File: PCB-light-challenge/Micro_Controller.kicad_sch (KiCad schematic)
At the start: 6 parts, among them J2 Screw_Terminal_01x20

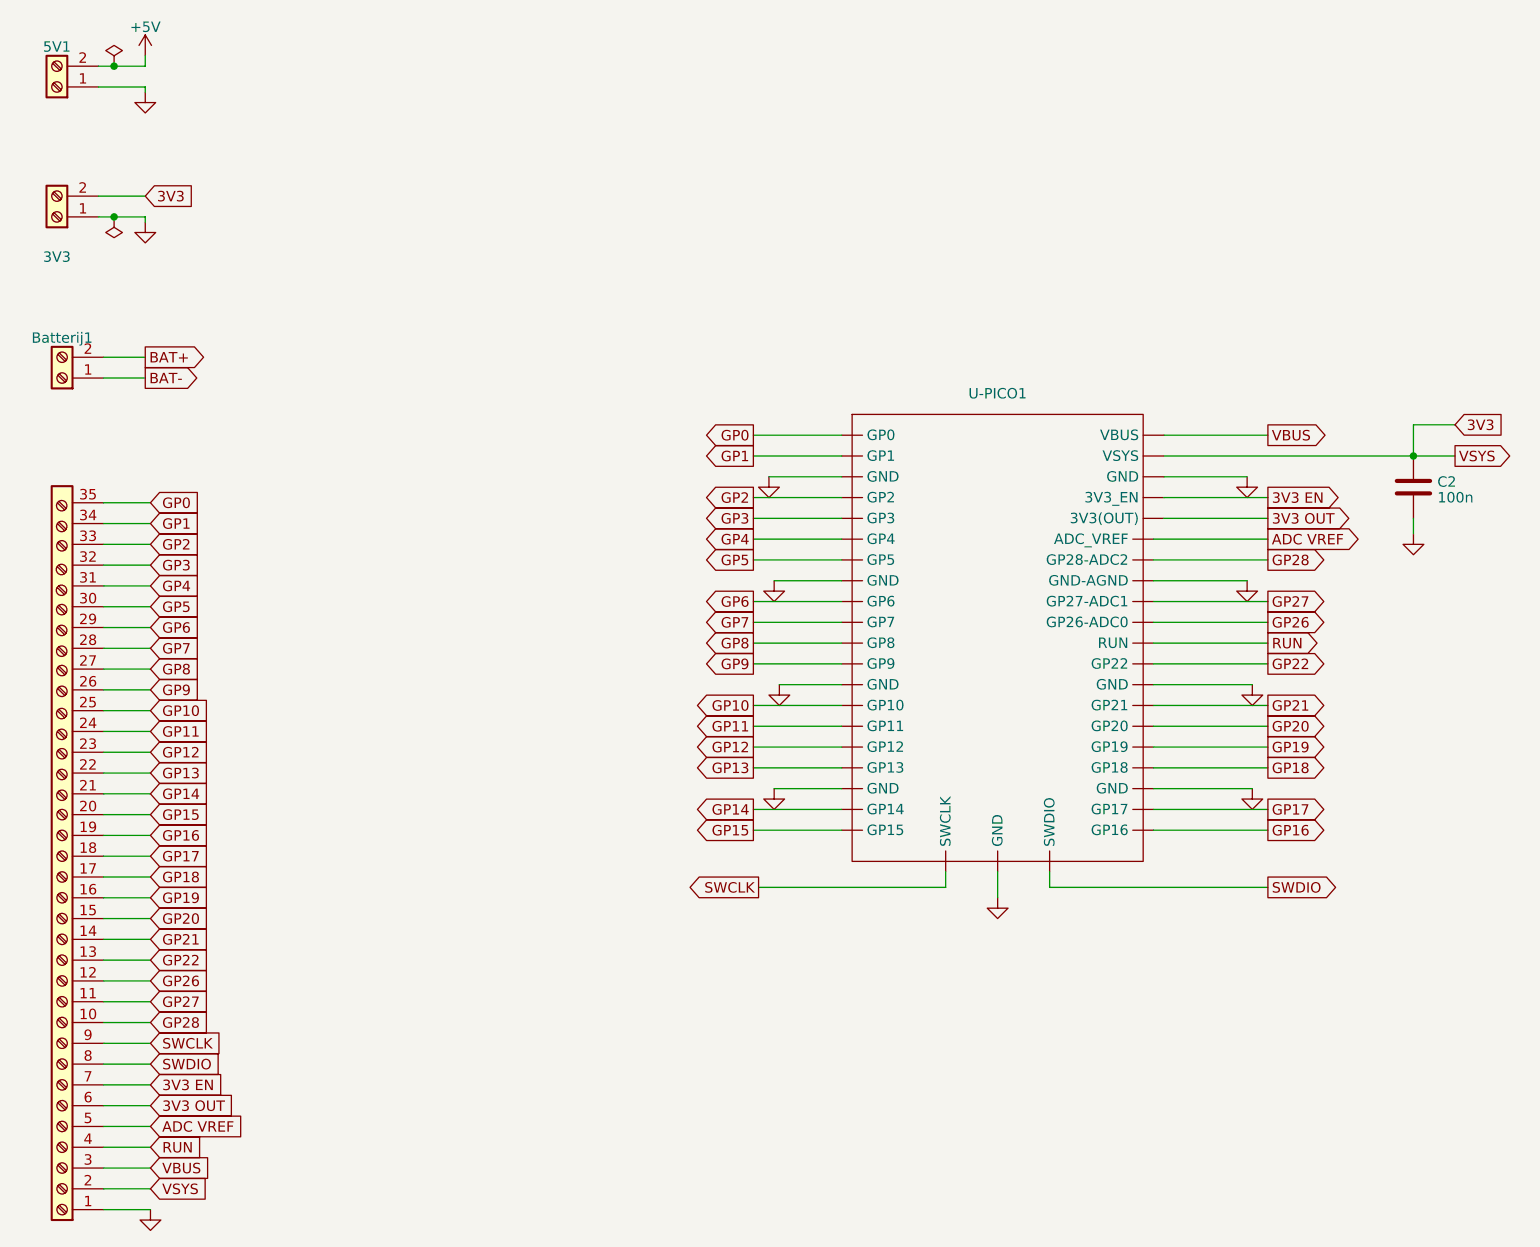
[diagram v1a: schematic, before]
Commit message: Mainboard onderdelen gesorteerd
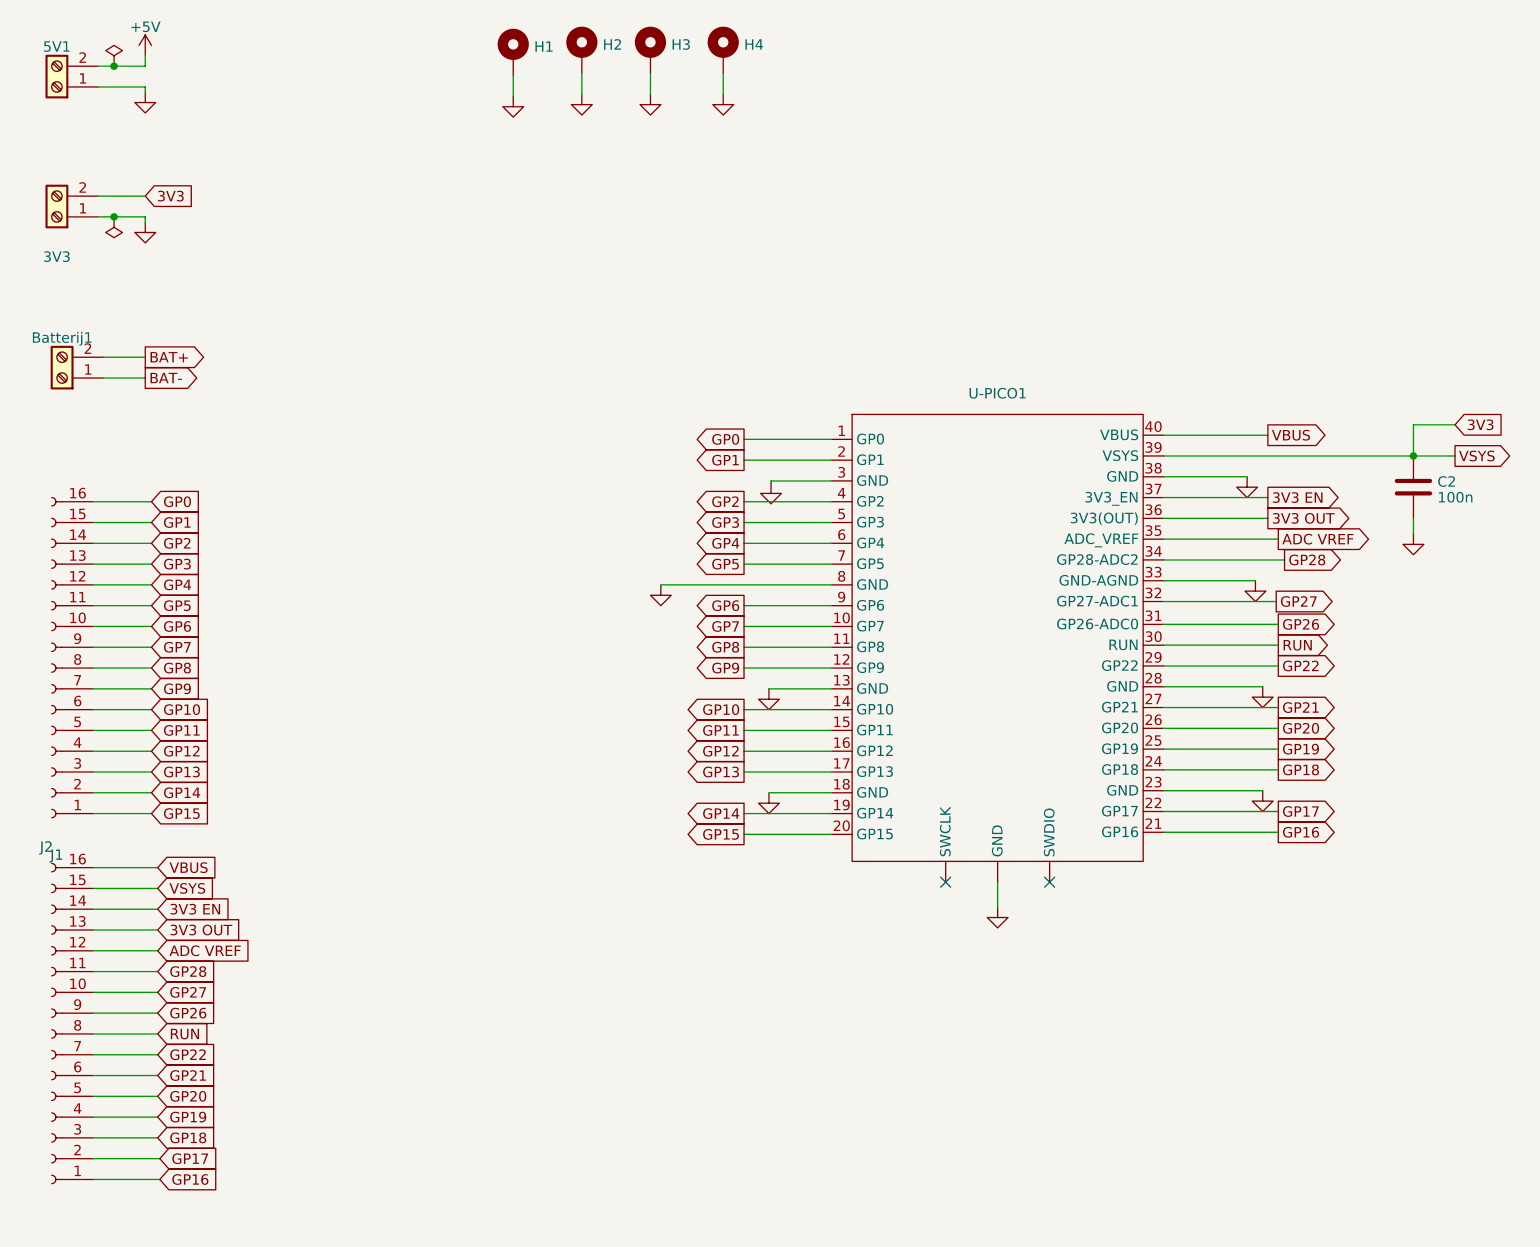
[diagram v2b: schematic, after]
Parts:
- removed J2: Screw_Terminal_01x20, Connector_PinHeader_2.54mm:PinHeader_1x35_P2.54mm_Horizontal, symbol Connector:Screw_Terminal_01x20
- added H1, H2, H3, H4: MountingHole_Pad, MountingHole:MountingHole_2.2mm_M2_DIN965_Pad, symbol Mechanical:MountingHole_Pad
- added J1, J2: Conn_01x16_Socket, Connector_PinHeader_2.54mm:PinHeader_1x16_P2.54mm_Vertical, symbol Connector:Conn_01x16_Socket
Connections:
- net SWCLK is gone; now on net GND: U-PICO1. (SWDIO)
- net SWDIO is gone; now on net GND: U-PICO1. (SWDIO)
- net 3V3: now also U-PICO1.39 (VSYS), J1.15 (Pin_15); no longer U-PICO1. (VSYS)
- net 3V3 EN: now also U-PICO1.37 (3V3_EN), J1.14 (Pin_14); no longer U-PICO1. (VSYS)
- net 3V3 OUT: now also U-PICO1.36 (3V3(OUT)), J1.13 (Pin_13); no longer U-PICO1. (VSYS)
- net ADC VREF: now also U-PICO1.35 (ADC_VREF), J1.12 (Pin_12); no longer U-PICO1. (VSYS)
- net GND: now also U-PICO1.13 (GND), U-PICO1.18 (GND), U-PICO1.23 (GND), U-PICO1.28 (GND), U-PICO1.3 (GND), U-PICO1.33 (GND-AGND), U-PICO1.38 (GND), U-PICO1.8 (GND), H1.1, H2.1, H3.1, H4.1
- net GP0: now also U-PICO1.1 (GP0), J2.16 (Pin_16); no longer U-PICO1. (VSYS)
- net GP1: now also U-PICO1.2 (GP1), J2.15 (Pin_15); no longer U-PICO1. (VSYS)
- net GP10: now also U-PICO1.14 (GP10), J2.6 (Pin_6); no longer U-PICO1. (VSYS)
- net GP11: now also U-PICO1.15 (GP11), J2.5 (Pin_5); no longer U-PICO1. (VSYS)
- net GP12: now also U-PICO1.16 (GP12), J2.4 (Pin_4); no longer U-PICO1. (VSYS)
- net GP13: now also U-PICO1.17 (GP13), J2.3 (Pin_3); no longer U-PICO1. (VSYS)
- net GP14: now also U-PICO1.19 (GP14), J2.2 (Pin_2); no longer U-PICO1. (VSYS)
- net GP15: now also U-PICO1.20 (GP15), J2.1 (Pin_1); no longer U-PICO1. (VSYS)
- net GP16: now also U-PICO1.21 (GP16), J1.1 (Pin_1); no longer U-PICO1. (VSYS)
- net GP17: now also U-PICO1.22 (GP17), J1.2 (Pin_2); no longer U-PICO1. (VSYS)
- net GP18: now also U-PICO1.24 (GP18), J1.3 (Pin_3); no longer U-PICO1. (VSYS)
- net GP19: now also U-PICO1.25 (GP19), J1.4 (Pin_4); no longer U-PICO1. (VSYS)
- net GP2: now also U-PICO1.4 (GP2), J2.14 (Pin_14); no longer U-PICO1. (VSYS)
- net GP20: now also U-PICO1.26 (GP20), J1.5 (Pin_5); no longer U-PICO1. (VSYS)
- net GP21: now also U-PICO1.27 (GP21), J1.6 (Pin_6); no longer U-PICO1. (VSYS)
- net GP22: now also U-PICO1.29 (GP22), J1.7 (Pin_7); no longer U-PICO1. (VSYS)
- net GP26: now also U-PICO1.31 (GP26-ADC0), J1.9 (Pin_9); no longer U-PICO1. (VSYS)
- net GP27: now also U-PICO1.32 (GP27-ADC1), J1.10 (Pin_10); no longer U-PICO1. (VSYS)
- net GP28: now also U-PICO1.34 (GP28-ADC2), J1.11 (Pin_11); no longer U-PICO1. (VSYS)
- net GP3: now also U-PICO1.5 (GP3), J2.13 (Pin_13); no longer U-PICO1. (VSYS)
- net GP4: now also U-PICO1.6 (GP4), J2.12 (Pin_12); no longer U-PICO1. (VSYS)
- net GP5: now also U-PICO1.7 (GP5), J2.11 (Pin_11); no longer U-PICO1. (VSYS)
- net GP6: now also U-PICO1.9 (GP6), J2.10 (Pin_10); no longer U-PICO1. (VSYS)
- net GP7: now also U-PICO1.10 (GP7), J2.9 (Pin_9); no longer U-PICO1. (VSYS)
- net GP8: now also U-PICO1.11 (GP8), J2.8 (Pin_8); no longer U-PICO1. (VSYS)
- net GP9: now also U-PICO1.12 (GP9), J2.7 (Pin_7); no longer U-PICO1. (VSYS)
- net RUN: now also U-PICO1.30 (RUN), J1.8 (Pin_8); no longer U-PICO1. (VSYS)
- net VBUS: now also U-PICO1.40 (VBUS), J1.16 (Pin_16); no longer U-PICO1. (VSYS)
- no-connect marks 0 -> 2

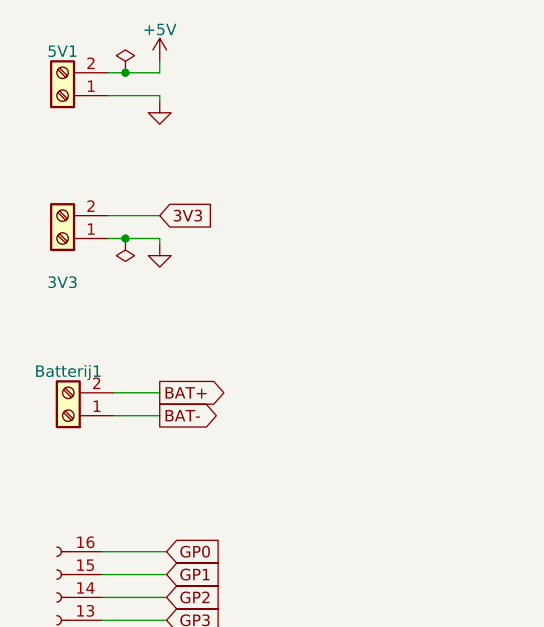
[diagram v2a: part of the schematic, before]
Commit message: main board aangepast en ground toegevoegd
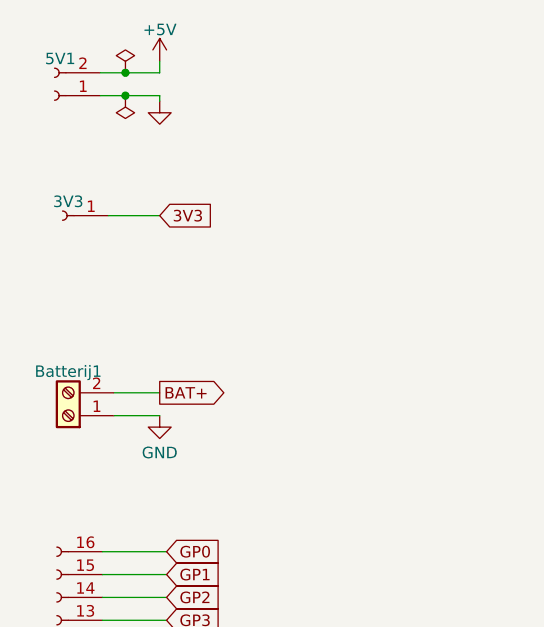
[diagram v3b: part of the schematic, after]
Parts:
- removed 3V3, 5V1: Screw_Terminal_01x02, Connector_PinHeader_2.54mm:PinHeader_1x02_P2.54mm_Horizontal, symbol Connector:Screw_Terminal_01x02
- added 3V3: Conn_01x01_Socket, Connector_PinHeader_2.54mm:PinHeader_1x01_P2.54mm_Vertical, symbol Connector:Conn_01x01_Socket
- added 5V1: Conn_01x02_Socket, Connector_PinHeader_2.54mm:PinHeader_1x02_P2.54mm_Vertical, symbol Connector:Conn_01x02_Socket
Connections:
- net BAT- is gone; now on net GND: Batterij1.1 (Pin_1)
- net +5V: now also 5V1.2 (Pin_2)
- net 3V3: now also 3V3.1 (Pin_1)
- net GND: now also 5V1.1 (Pin_1)
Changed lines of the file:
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@@
     (company "HHS Living Labs")
   )
-  (junction (at 35.56 49.53) (diameter 0) (color 0 0 0 0)
+  (junction (at 35.56 33.655) (diameter 0) (color 0 0 0 0)
   )
   (junction (at 194.31 78.74) (diameter 0) (color 0 0 0 0)
@@
     (stroke (width 0) (type default))
   )
-  (wire (pts (xy 35.56 49.53) (xy 39.37 49.53))
-    (stroke (width 0) (type default))
-  )
   (wire (pts (xy 33.02 136.652) (xy 40.894 136.652))
     (stroke (width 0) (type default))
   )
-  (wire (pts (xy 33.655 31.115) (xy 35.56 31.115))
+  (wire (pts (xy 32.766 31.115) (xy 35.56 31.115))
     (stroke (width 0) (type default))
   )
@@
     (stroke (width 0) (type default))
   )
+  (wire (pts (xy 35.56 33.655) (xy 39.37 33.655))
+    (stroke (width 0) (type default))
+  )
   (wire (pts (xy 112.522 76.708) (xy 123.19 76.708))
     (stroke (width 0) (type default))
@@
     (stroke (width 0) (type default))
   )
-  (wire (pts (xy 39.37 50.165) (xy 39.37 49.53))
-    (stroke (width 0) (type default))
-  )
   (wire (pts (xy 33.02 164.592) (xy 41.148 164.592))
     (stroke (width 0) (type default))
@@
     (stroke (width 0) (type default))
   )
-  (wire (pts (xy 33.655 49.53) (xy 35.56 49.53))
-    (stroke (width 0) (type default))
-  )
   (wire (pts (xy 34.29 66.675) (xy 39.37 66.675))
     (stroke (width 0) (type default))
@@
     (stroke (width 0) (type default))
   )
-  (wire (pts (xy 33.655 33.655) (xy 39.37 33.655))
+  (wire (pts (xy 32.766 33.655) (xy 35.56 33.655))
     (stroke (width 0) (type default))
   )
@@
     )
   )
-  (global_label "BAT-" (shape output) (at 39.37 69.215 0) (fields_autoplaced)
-    (effects (font (size 1.27 1.27)) (justify left))
-    (property "Intersheetrefs" "${INTERSHEET_REFS}" (at 47.1744 69.215 0)
-      (effects (font (size 1.27 1.27)) (justify left) hide)
-    )
-  )
   (global_label "GP20" (shape output) (at 177.8 112.014 0) (fields_autoplaced)
     (effects (font (size 1.27 1.27)) (justify left))
@@
     )
   )
-  (symbol (lib_name "Screw_Terminal_01x02_1") (lib_id "Connector:Screw_Terminal_01x02") (at 28.575 49.53 180) (unit 1)
-    (in_bom yes) (on_board yes) (dnp no) (fields_autoplaced)
-    (property "Reference" "3V3" (at 28.575 54.4289 0)
+  (symbol (lib_id "Connector:Conn_01x02_Socket") (at 27.686 33.655 180) (unit 1)
+    (in_bom yes) (on_board yes) (dnp no) (fields_autoplaced)
+    (property "Reference" "5V1" (at 28.321 29.5689 0)
       (effects (font (size 1.27 1.27)))
     )
-    (property "Value" "Screw_Terminal_01x02" (at 28.575 54.4289 0)
-      (effects (font (size 1.27 1.27)) hide)
-    )
-    (property "Footprint" "Connector_PinHeader_2.54mm:PinHeader_1x02_P2.54mm_Horizontal" (at 28.321 52.324 0)
-      (effects (font (size 1.27 1.27)) hide)
-    )
-    (property "Datasheet" "~" (at 28.575 49.53 0)
+    (property "Value" "Conn_01x02_Socket" (at 28.321 29.5689 0)
+      (effects (font (size 1.27 1.27)) hide)
+    )
+    (property "Footprint" "Connector_PinHeader_2.54mm:PinHeader_1x02_P2.54mm_Vertical" (at 27.686 33.655 0)
+      (effects (font (size 1.27 1.27)) hide)
+    )
+    (property "Datasheet" "~" (at 27.686 33.655 0)
       (effects (font (size 1.27 1.27)) hide)
     )
@@
       (project "PCB-light-challenge"
         (path "/35573e8f-7834-430c-81d2-239f316c7834/2e4391fc-91c5-40c6-9f1e-d883ea305622"
-          (reference "3V3") (unit 1)
+          (reference "5V1") (unit 1)
         )
       )
@@
     )
   )
+  (symbol (lib_id "power:GND") (at 39.37 69.215 0) (unit 1)
+    (in_bom yes) (on_board yes) (dnp no) (fields_autoplaced)
+    (property "Reference" "#PWR018" (at 39.37 75.565 0)
+      (effects (font (size 1.27 1.27)) hide)
+    )
+    (property "Value" "GND" (at 39.37 73.3505 0)
+      (effects (font (size 1.27 1.27)))
+    )
+    (property "Footprint" "" (at 39.37 69.215 0)
+      (effects (font (size 1.27 1.27)) hide)
+    )
+    (property "Datasheet" "" (at 39.37 69.215 0)
+      (effects (font (size 1.27 1.27)) hide)
+    )
+    (pin "1")
+    (instances
+      (project "PCB-light-challenge"
+        (path "/35573e8f-7834-430c-81d2-239f316c7834/2e4391fc-91c5-40c6-9f1e-d883ea305622"
+          (reference "#PWR018") (unit 1)
+        )
+      )
+    )
+  )
   (symbol (lib_id "power:GND") (at 175.895 106.934 0) (unit 1)
     (in_bom yes) (on_board yes) (dnp no) (fields_autoplaced)
@@
     (pin "")
     (pin "1")
+    (pin "10")
     (pin "11")
     (pin "12")
@@
     (pin "18")
     (pin "19")
+    (pin "2")
     (pin "20")
-    (pin "2")
     (pin "21")
     (pin "22")
@@
     (pin "8")
     (pin "9")
-    (pin "10")
     (instances
       (project "PCB-light-challenge"
@@
     )
   )
+  (symbol (lib_id "Connector:Conn_01x01_Socket") (at 28.575 46.99 180) (unit 1)
+    (in_bom yes) (on_board yes) (dnp no) (fields_autoplaced)
+    (property "Reference" "3V3" (at 29.21 45.4439 0)
+      (effects (font (size 1.27 1.27)))
+    )
+    (property "Value" "Conn_01x01_Socket" (at 29.21 45.4439 0)
+      (effects (font (size 1.27 1.27)) hide)
+    )
+    (property "Footprint" "Connector_PinHeader_2.54mm:PinHeader_1x01_P2.54mm_Vertical" (at 28.575 46.99 0)
+      (effects (font (size 1.27 1.27)) hide)
+    )
+    (property "Datasheet" "~" (at 28.575 46.99 0)
+      (effects (font (size 1.27 1.27)) hide)
+    )
+    (pin "1")
+    (instances
+      (project "PCB-light-challenge"
+        (path "/35573e8f-7834-430c-81d2-239f316c7834/2e4391fc-91c5-40c6-9f1e-d883ea305622"
+          (reference "3V3") (unit 1)
+        )
+      )
+    )
+  )
+  (symbol (lib_id "power:PWR_FLAG") (at 35.56 33.655 180) (unit 1)
+    (in_bom yes) (on_board yes) (dnp no) (fields_autoplaced)
+    (property "Reference" "#FLG01" (at 35.56 35.56 0)
+      (effects (font (size 1.27 1.27)) hide)
+    )
+    (property "Value" "PWR_FLAG" (at 35.56 37.1569 0)
+      (effects (font (size 1.27 1.27)) hide)
+    )
+    (property "Footprint" "" (at 35.56 33.655 0)
+      (effects (font (size 1.27 1.27)) hide)
+    )
+    (property "Datasheet" "~" (at 35.56 33.655 0)
+      (effects (font (size 1.27 1.27)) hide)
+    )
+    (pin "1")
+    (instances
+      (project "PCB-light-challenge"
+        (path "/35573e8f-7834-430c-81d2-239f316c7834/2e4391fc-91c5-40c6-9f1e-d883ea305622"
+          (reference "#FLG01") (unit 1)
+        )
+      )
+    )
+  )
   (symbol (lib_id "power:GND") (at 115.57 107.188 0) (unit 1)
     (in_bom yes) (on_board yes) (dnp no) (fields_autoplaced)
@@
         (path "/35573e8f-7834-430c-81d2-239f316c7834/2e4391fc-91c5-40c6-9f1e-d883ea305622"
           (reference "#PWR014") (unit 1)
-        )
-      )
-    )
-  )
-  (symbol (lib_id "power:PWR_FLAG") (at 35.56 49.53 180) (unit 1)
-    (in_bom yes) (on_board yes) (dnp no) (fields_autoplaced)
-    (property "Reference" "#FLG01" (at 35.56 51.435 0)
-      (effects (font (size 1.27 1.27)) hide)
-    )
-    (property "Value" "PWR_FLAG" (at 35.56 53.0319 0)
-      (effects (font (size 1.27 1.27)) hide)
-    )
-    (property "Footprint" "" (at 35.56 49.53 0)
-      (effects (font (size 1.27 1.27)) hide)
-    )
-    (property "Datasheet" "~" (at 35.56 49.53 0)
-      (effects (font (size 1.27 1.27)) hide)
-    )
-    (pin "1")
-    (instances
-      (project "PCB-light-challenge"
-        (path "/35573e8f-7834-430c-81d2-239f316c7834/2e4391fc-91c5-40c6-9f1e-d883ea305622"
-          (reference "#FLG01") (unit 1)
         )
       )
@@
     )
   )
-  (symbol (lib_id "power:GND") (at 39.37 50.165 0) (unit 1)
-    (in_bom yes) (on_board yes) (dnp no) (fields_autoplaced)
-    (property "Reference" "#PWR020" (at 39.37 56.515 0)
-      (effects (font (size 1.27 1.27)) hide)
-    )
-    (property "Value" "GND" (at 39.37 54.3005 0)
-      (effects (font (size 1.27 1.27)) hide)
-    )
-    (property "Footprint" "" (at 39.37 50.165 0)
-      (effects (font (size 1.27 1.27)) hide)
-    )
-    (property "Datasheet" "" (at 39.37 50.165 0)
-      (effects (font (size 1.27 1.27)) hide)
-    )
-    (pin "1")
-    (instances
-      (project "PCB-light-challenge"
-        (path "/35573e8f-7834-430c-81d2-239f316c7834/2e4391fc-91c5-40c6-9f1e-d883ea305622"
-          (reference "#PWR020") (unit 1)
-        )
-      )
-    )
-  )
   (symbol (lib_id "power:GND") (at 101.092 34.544 0) (unit 1)
     (in_bom yes) (on_board yes) (dnp no) (fields_autoplaced)
@@
         )
       )
-    )
-  )
-  (symbol (lib_id "Connector:Screw_Terminal_01x02") (at 28.575 33.655 180) (unit 1)
-    (in_bom yes) (on_board yes) (dnp no) (fields_autoplaced)
-    (property "Reference" "5V1" (at 28.575 28.7561 0)
-      (effects (font (size 1.27 1.27)))
-    )
-    (property "Value" "Screw_Terminal_01x02" (at 28.575 28.7561 0)
-      (effects (font (size 1.27 1.27)) hide)
-    )
-    (property "Footprint" "Connector_PinHeader_2.54mm:PinHeader_1x02_P2.54mm_Horizontal" (at 28.575 33.655 0)
-      (effects (font (size 1.27 1.27)) hide)
-    )
-    (property "Datasheet" "~" (at 28.575 33.655 0)
-      (effects (font (size 1.27 1.27)) hide)
-    )
-    (pin "1")
-    (pin "2")
-    (instances
-      (project "PCB-light-challenge"
-        (path "/35573e8f-7834-430c-81d2-239f316c7834/2e4391fc-91c5-40c6-9f1e-d883ea305622"
-          (reference "5V1") (unit 1)
-        )
-      )
